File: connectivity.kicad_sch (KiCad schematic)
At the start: 3 parts

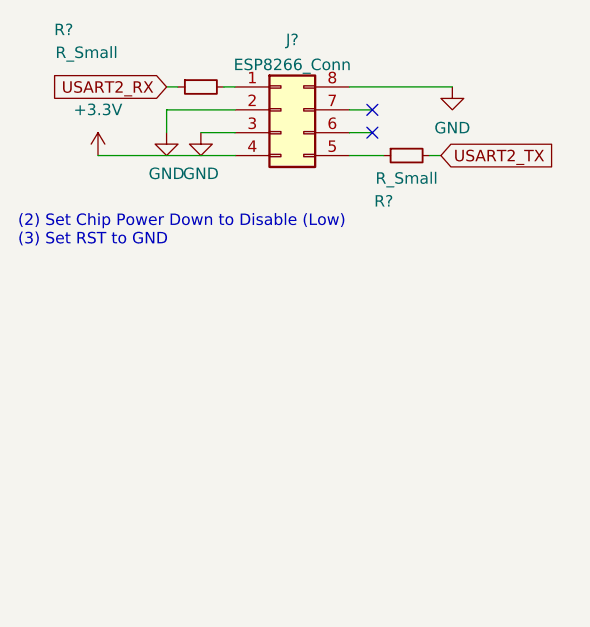
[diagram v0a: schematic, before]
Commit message: added NUF2030 footprint and symbol
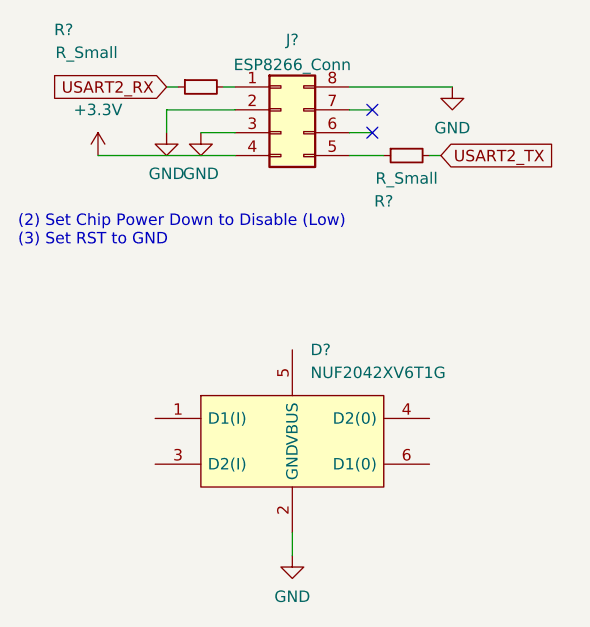
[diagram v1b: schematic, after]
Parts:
- added D?: NUF2042XV6T1G, CustomKeyboard:SOTFL50P160X60-6N, symbol CustomKeyboard:NUF2042XV6T1G
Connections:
- net GND: now also D?.2 (GND)
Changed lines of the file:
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@@
+    (stroke (width 0) (type default) (color 0 0 0 0))
+  )
+  (wire (pts (xy 45.72 71.12) (xy 45.72 73.66))
     (stroke (width 0) (type default) (color 0 0 0 0))
   )
@@
     )
   )
+  (symbol (lib_id "power:GND") (at 45.72 73.66 0) (unit 1)
+    (in_bom yes) (on_board yes) (fields_autoplaced)
+    (property "Reference" "#PWR?" (id 0) (at 45.72 80.01 0)
+      (effects (font (size 1.27 1.27)) hide)
+    )
+    (property "Value" "GND" (id 1) (at 45.72 78.2225 0))
+    (property "Footprint" "" (id 2) (at 45.72 73.66 0)
+      (effects (font (size 1.27 1.27)) hide)
+    )
+    (property "Datasheet" "" (id 3) (at 45.72 73.66 0)
+      (effects (font (size 1.27 1.27)) hide)
+    )
+    (pin "1")
+  )
   (symbol (lib_id "power:GND") (at 63.5 21.59 0) (unit 1)
     (in_bom yes) (on_board yes) (fields_autoplaced)
@@
     (pin "1")
   )
+  (symbol (lib_id "CustomKeyboard:NUF2042XV6T1G") (at 30.48 58.42 0) (unit 1)
+    (in_bom yes) (on_board yes) (fields_autoplaced)
+    (property "Reference" "D?" (id 0) (at 47.7394 50.8 0)
+      (effects (font (size 1.27 1.27)) (justify left))
+    )
+    (property "Value" "NUF2042XV6T1G" (id 1) (at 47.7394 53.34 0)
+      (effects (font (size 1.27 1.27)) (justify left))
+    )
+    (property "Footprint" "CustomKeyboard:SOTFL50P160X60-6N" (id 2) (at 57.15 55.88 0)
+      (effects (font (size 1.27 1.27)) (justify left) hide)
+    )
+    (property "Datasheet" "http://www.onsemi.com/pub/Collateral/NUF2030XV6-D.PDF" (id 3) (at 57.15 58.42 0)
+      (effects (font (size 1.27 1.27)) (justify left) hide)
+    )
+    (property "Description" "ESD Suppressors / TVS Diodes USB UPSTR FTR IN" (id 4) (at 57.15 60.96 0)
+      (effects (font (size 1.27 1.27)) (justify left) hide)
+    )
+    (property "Height" "0.6" (id 5) (at 57.15 63.5 0)
+      (effects (font (size 1.27 1.27)) (justify left) hide)
+    )
+    (property "Mouser Part Number" "863-NUF2042XV6T1G" (id 6) (at 57.15 66.04 0)
+      (effects (font (size 1.27 1.27)) (justify left) hide)
+    )
+    (property "Mouser Price/Stock" "https://www.mouser.co.uk/ProductDetail/onsemi/NUF2042XV6T1G?qs=ZXBb0xZ9WeAV3XcAwewBSw%3D%3D" (id 7) (at 57.15 68.58 0)
+      (effects (font (size 1.27 1.27)) (justify left) hide)
+    )
+    (property "Manufacturer_Name" "onsemi" (id 8) (at 57.15 71.12 0)
+      (effects (font (size 1.27 1.27)) (justify left) hide)
+    )
+    (property "Manufacturer_Part_Number" "NUF2042XV6T1G" (id 9) (at 57.15 73.66 0)
+      (effects (font (size 1.27 1.27)) (justify left) hide)
+    )
+    (pin "1")
+    (pin "2")
+    (pin "3")
+    (pin "4")
+    (pin "5")
+    (pin "6")
+  )
   (symbol (lib_id "power:+3.3V") (at 24.13 29.21 0) (unit 1)
